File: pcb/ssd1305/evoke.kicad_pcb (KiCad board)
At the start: 2 copper layers, 60 x 45 mm, 19 parts, among them U1 STM32F103C8Tx

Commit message: Fix bug with pins being wrong on connector, and add USART header
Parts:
- added J1: Conn_01x03_Male, Connector_PinHeader_2.54mm:PinHeader_1x03_P2.54mm_Vertical, F.Cu at (123.7, 58.9)
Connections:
- LCD_CONN1 pad 20: +3V3 -> GND
- LCD_CONN1 pad 21: GND -> +3V3
- U1 pad 30: Net-(U1-Pad30) -> USART1_TX
- U1 pad 31: Net-(U1-Pad31) -> USART1_RX
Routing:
- net USART1_TX: track 0.00 -> 20.7 mm, vias 0 -> 1
- net USART1_RX: track 0.00 -> 20.4 mm, vias 0 -> 1
- net GND: track 62.0 -> 58.7 mm, vias 14 -> 13
- net SWCLK: track 9.55 -> 8.17 mm
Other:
- board text added: "RX"
- board text added: "TX"

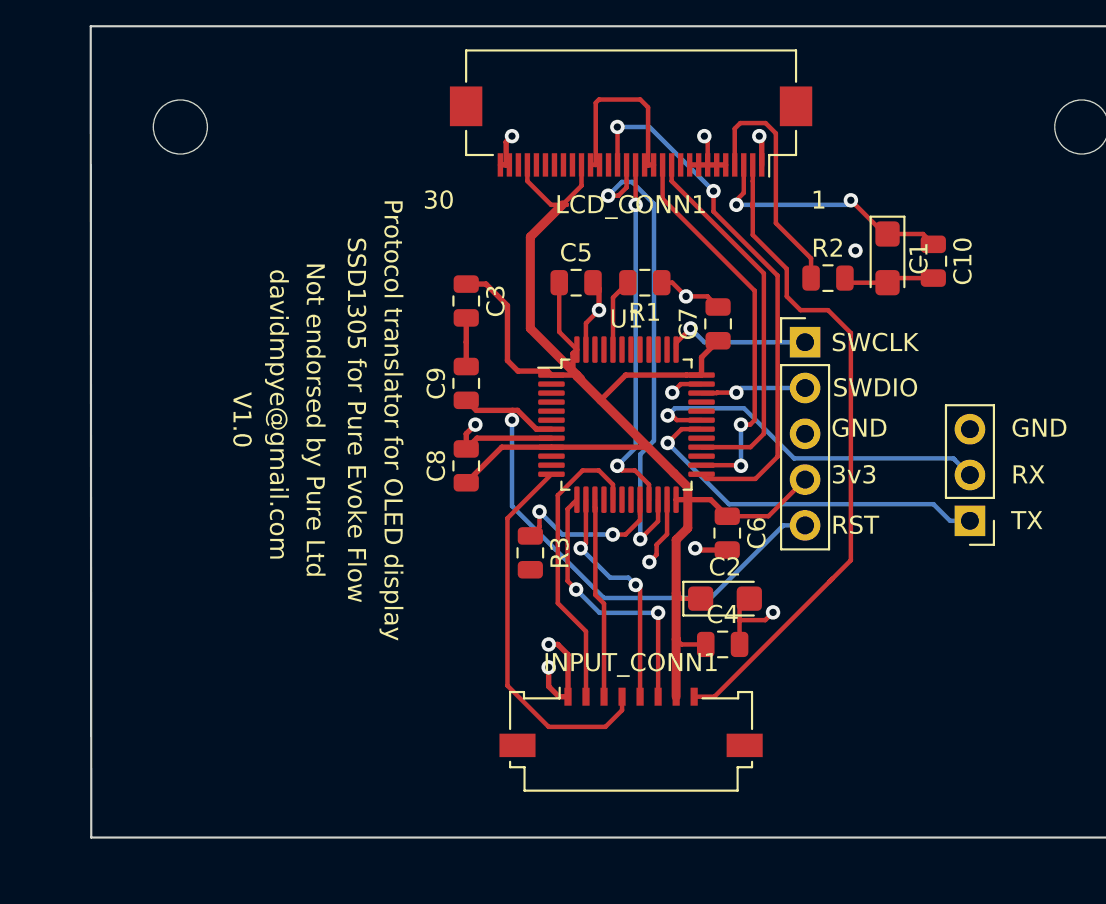
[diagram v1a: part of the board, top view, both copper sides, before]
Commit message: Addition of additional components as per jack wan's schematic example
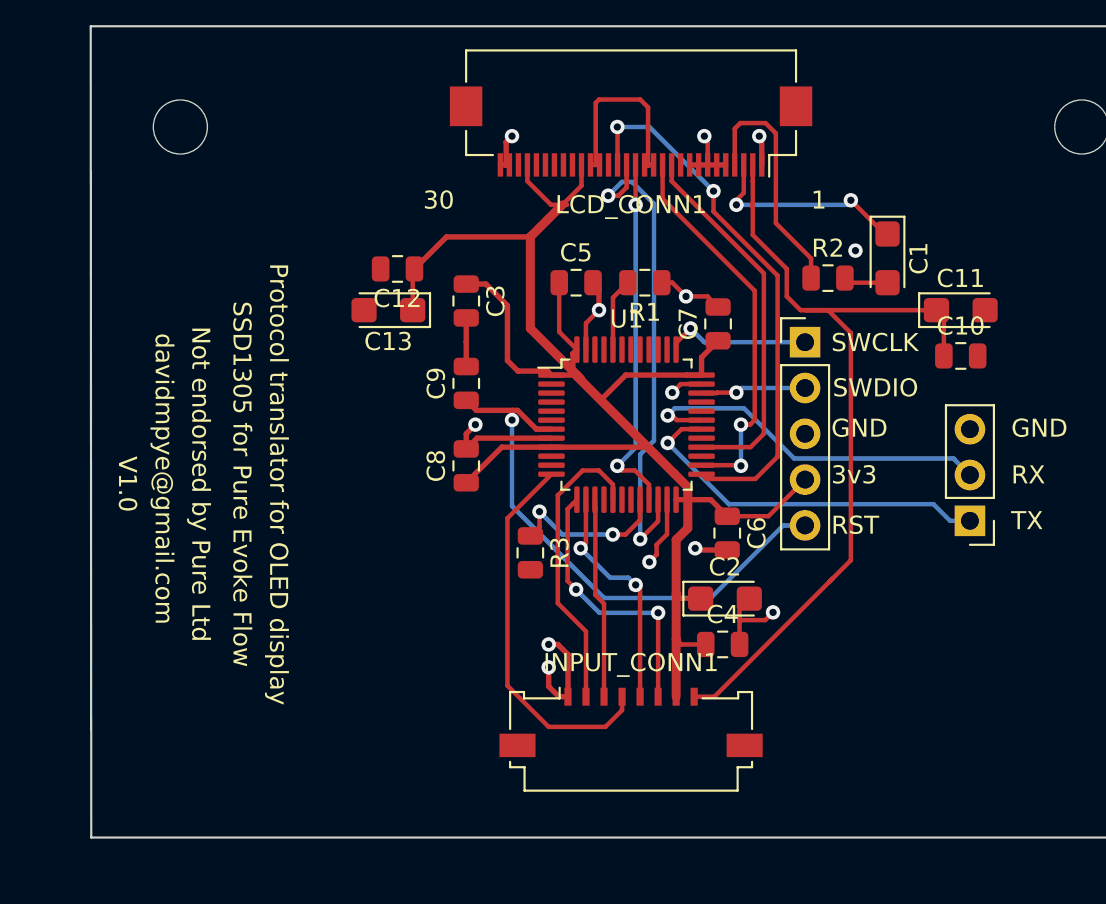
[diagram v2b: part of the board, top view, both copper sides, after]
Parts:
- added C11: 10uF, Capacitor_Tantalum_SMD:CP_EIA-3216-18_Kemet-A, F.Cu at (123.2, 47.2)
- added C12: 100nF, Capacitor_SMD:C_0805_2012Metric, F.Cu at (91.9, 45.0)
- added C13: 4.7uF, Capacitor_Tantalum_SMD:CP_EIA-3216-18_Kemet-A, F.Cu at (91.4, 47.2)
- C1: value 10uF -> 4.7uF
- moved C10 5.47 mm to (123.2, 49.8), turned to 0 degrees
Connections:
- C10 pad 1: Net-(C1-Pad1) -> VCC
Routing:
- net VCC: track 37.4 -> 47.4 mm
- net +3V3: track 88.6 -> 98.2 mm
- net Net-(C1-Pad1): track 14.6 -> 11.8 mm
- net GND: track 58.7 -> 56.4 mm

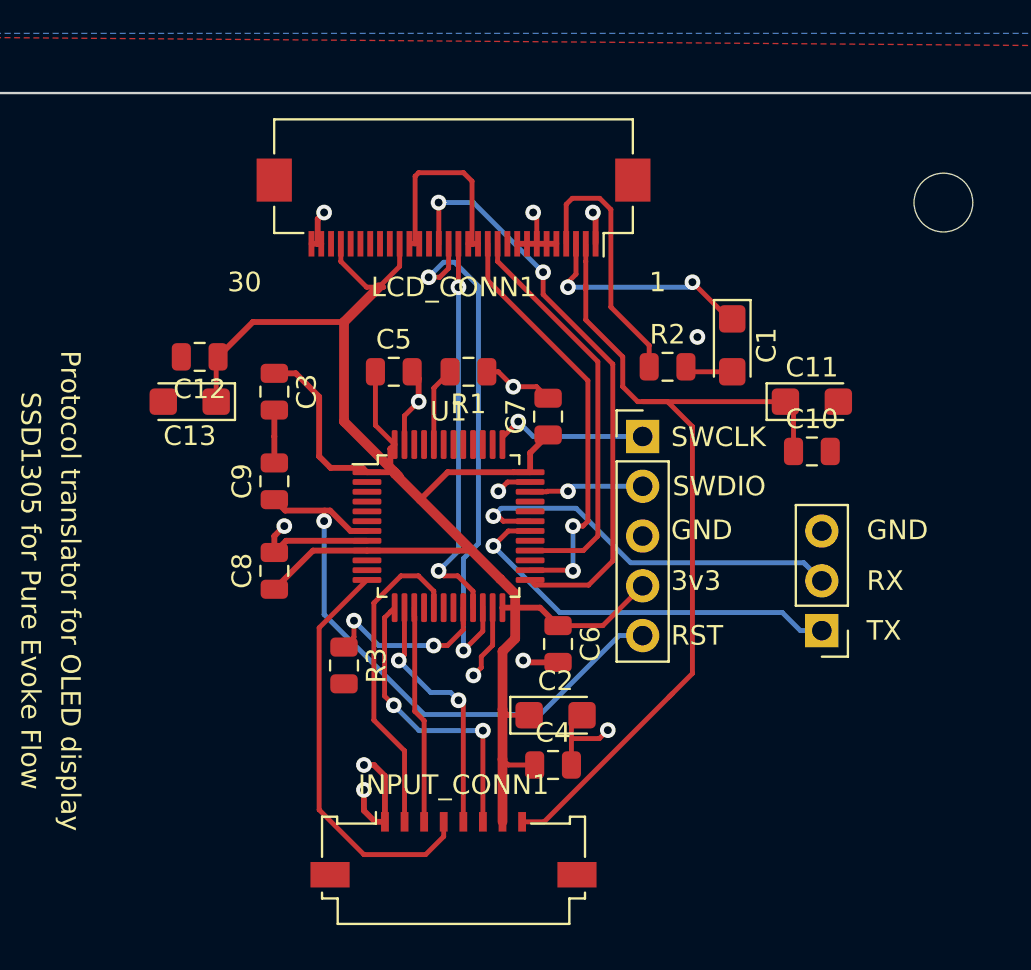
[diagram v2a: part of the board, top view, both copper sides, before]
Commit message: Put next revision into manufacture - hopefully ready to go, now with test points!
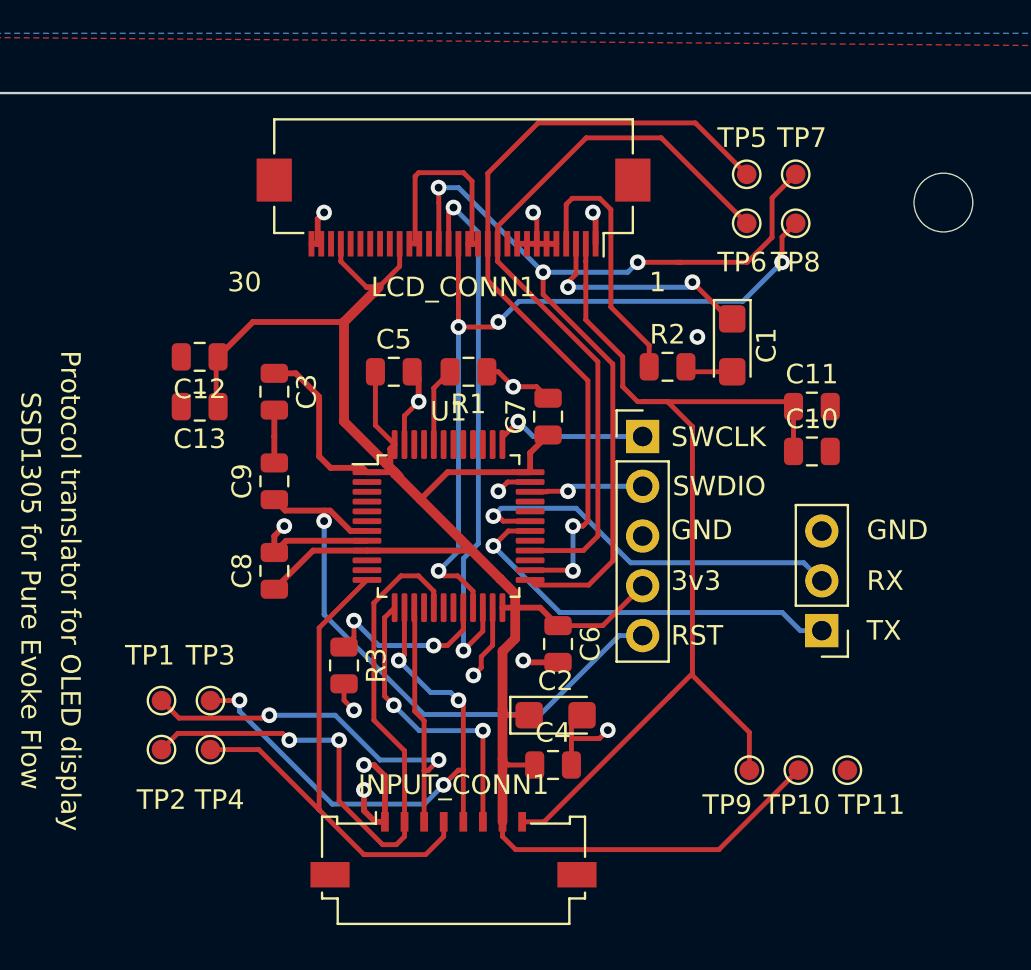
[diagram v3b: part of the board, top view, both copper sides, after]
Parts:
- added TP1: TestPoint, TestPoint:TestPoint_Pad_D1.0mm, F.Cu at (90.0, 62.5)
- added TP10: TestPoint, TestPoint:TestPoint_Pad_D1.0mm, F.Cu at (122.5, 66.0)
- added TP11: TestPoint, TestPoint:TestPoint_Pad_D1.0mm, F.Cu at (125.0, 66.0)
- added TP2: TestPoint, TestPoint:TestPoint_Pad_D1.0mm, F.Cu at (90.0, 65.0)
- added TP3: TestPoint, TestPoint:TestPoint_Pad_D1.0mm, F.Cu at (92.5, 62.5)
- added TP4: TestPoint, TestPoint:TestPoint_Pad_D1.0mm, F.Cu at (92.5, 65.0)
- added TP5: TestPoint, TestPoint:TestPoint_Pad_D1.0mm, F.Cu at (119.9, 35.6)
- added TP6: TestPoint, TestPoint:TestPoint_Pad_D1.0mm, F.Cu at (119.9, 38.1)
- added TP7: TestPoint, TestPoint:TestPoint_Pad_D1.0mm, F.Cu at (122.4, 35.6)
- added TP8: TestPoint, TestPoint:TestPoint_Pad_D1.0mm, F.Cu at (122.4, 38.1)
- added TP9: TestPoint, TestPoint:TestPoint_Pad_D1.0mm, F.Cu at (120.0, 66.0)
- C11, C13: footprint Capacitor_Tantalum_SMD:CP_EIA-3216-18_Kemet-A -> Capacitor_SMD:C_0805_2012Metric
- R2: value 1.5M -> 1.2M
- moved C13 0.57 mm to (91.9, 47.5)
- moved C11 0.25 mm to (123.2, 47.5)
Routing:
- net LCD_D_C: track 20.1 -> 40.3 mm, vias 2 -> 4
- net LCD_SCK: track 21.6 -> 40.6 mm
- net SDIN_IN: track 16.6 -> 34.5 mm, vias 0 -> 2
- net LCD_CS: track 30.0 -> 47.4 mm, vias 2 -> 3
- net +3V3: track 98.2 -> 115.6 mm
- net LCD_DATA: track 20.8 -> 38.1 mm
- net SCK_IN: track 11.1 -> 27.6 mm, vias 0 -> 2
- net CS_IN: track 13.1 -> 29.3 mm, vias 2 -> 4
- net D_C_IN: track 21.2 -> 28.0 mm
- net VCC: track 47.4 -> 53.6 mm
- net GND: track 56.4 -> 57.9 mm, vias 13 -> 14
- net LCD_RST: track 27.3 -> 28.0 mm

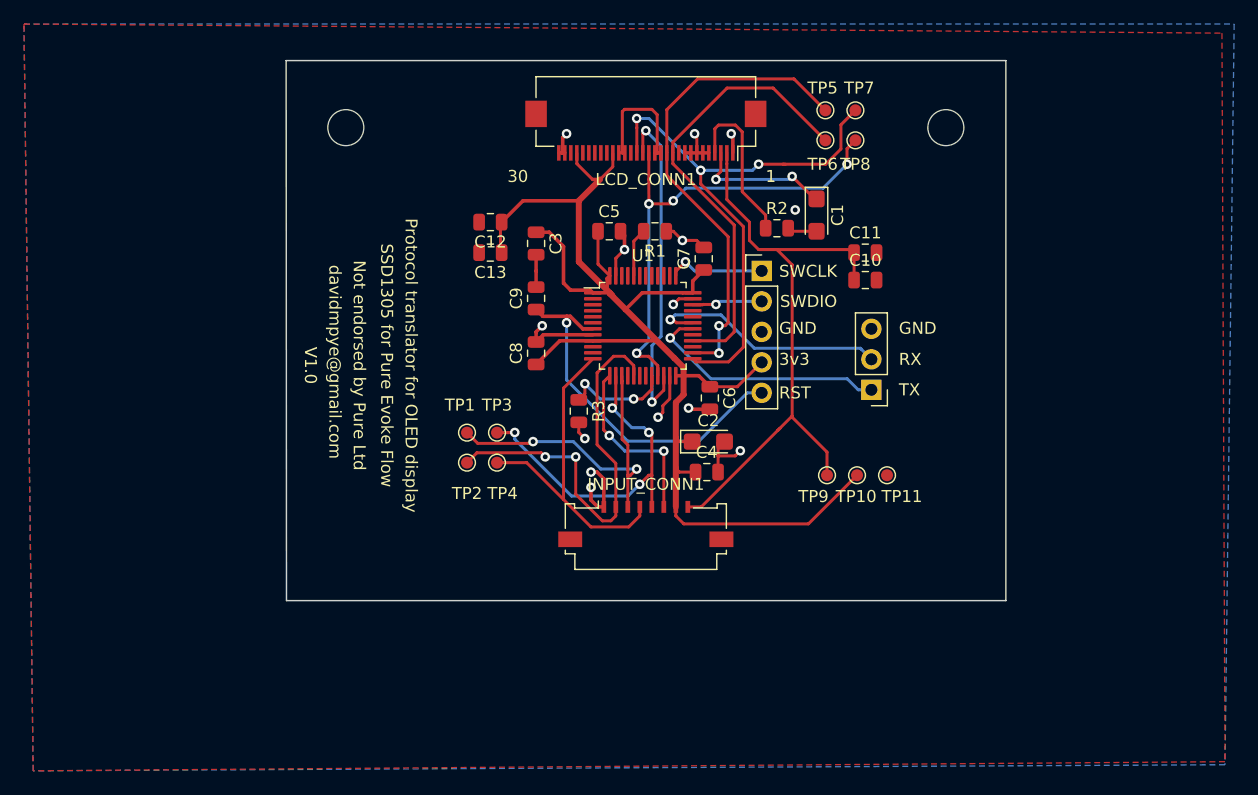
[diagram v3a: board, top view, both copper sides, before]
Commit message: Update to version 1.1 of OLED PCB with square THT TP pads
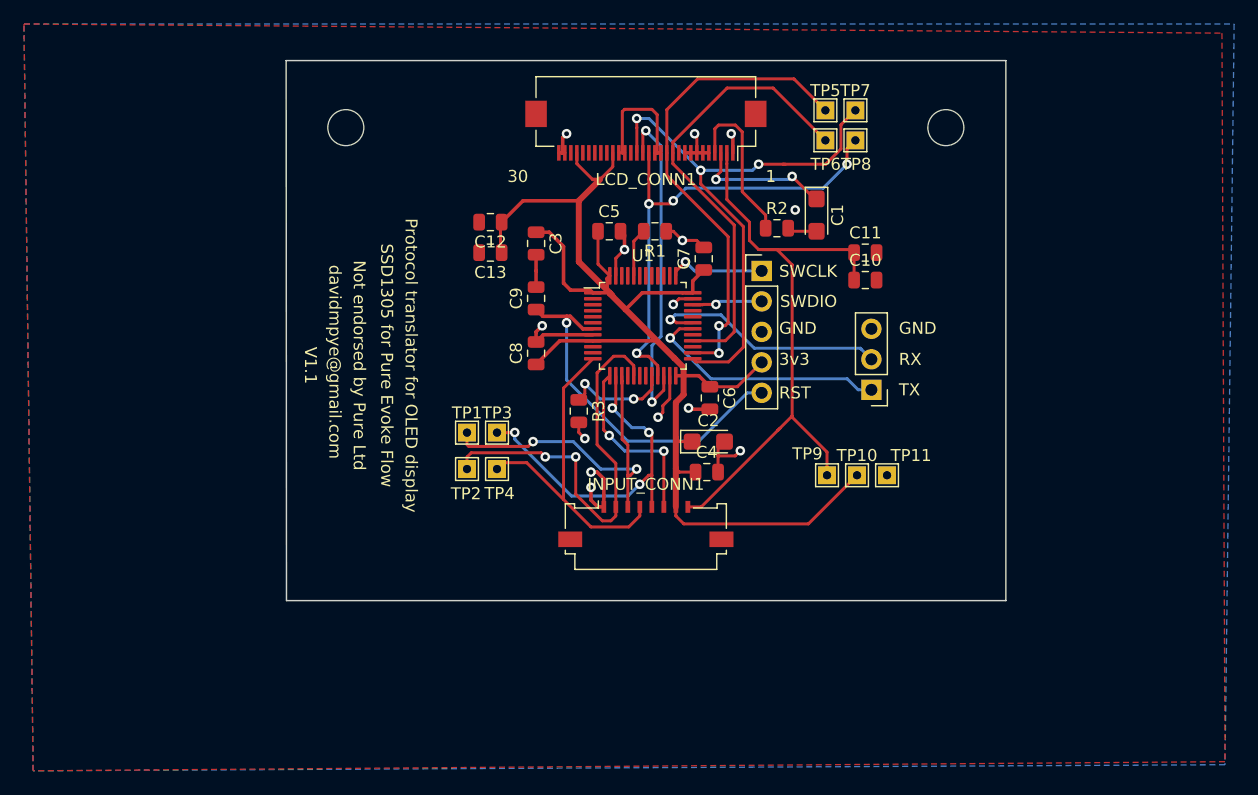
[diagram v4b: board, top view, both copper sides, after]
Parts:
- TP1, TP10, TP11, TP2, TP3, TP4, TP5, TP6, TP7, TP8, TP9: footprint TestPoint:TestPoint_Pad_D1.0mm -> TestPoint:TestPoint_THTPad_1.5x1.5mm_Drill0.7mm
- moved TP2 0.53 mm to (90.0, 65.5)
- moved TP4 0.53 mm to (92.5, 65.5)
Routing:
- net SCK_IN: track 27.6 -> 28.4 mm
- net SDIN_IN: track 34.5 -> 35.3 mm
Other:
- board text added: "V1.1"
- board text removed: "V1.0"
